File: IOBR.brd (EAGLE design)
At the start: 53.3 x 53.3 mm, 10 parts, among them J1 Digital_0_7, J10 Power, J2 Analog, J3 Digital_8_13

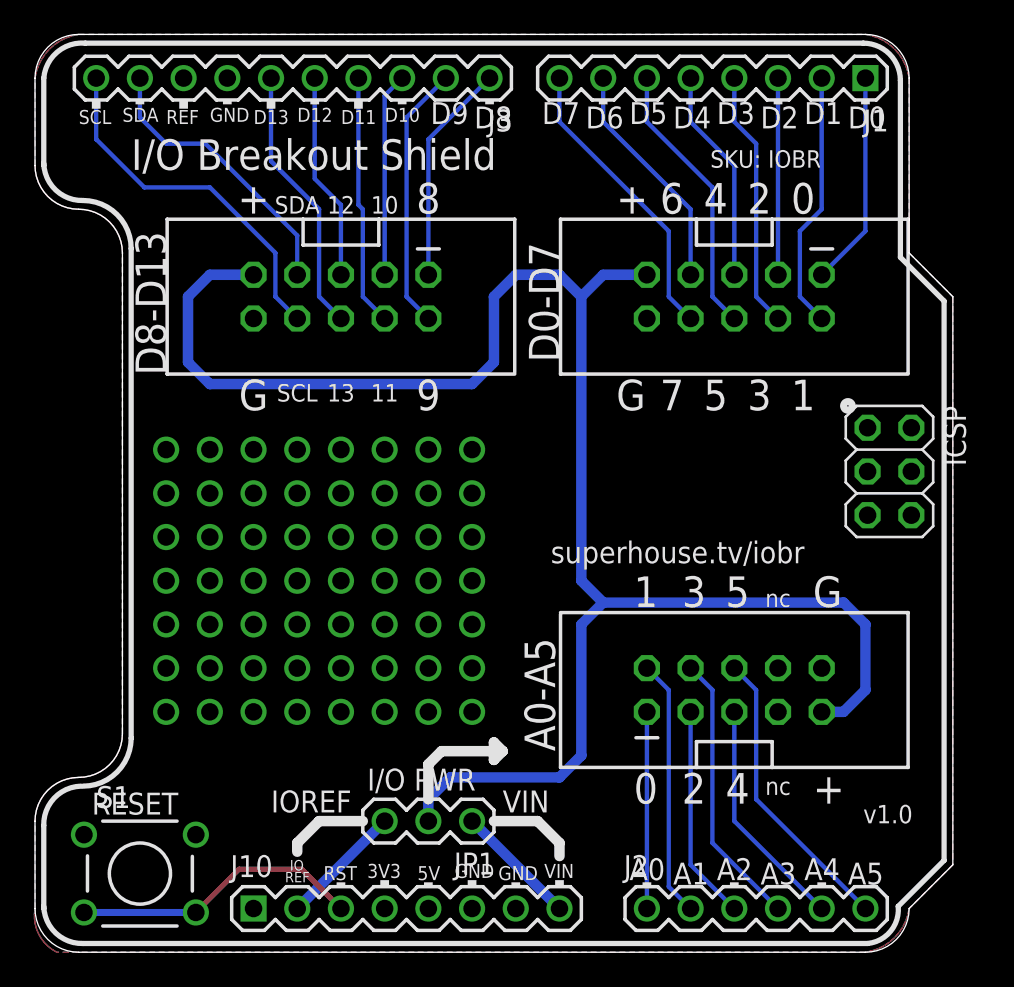
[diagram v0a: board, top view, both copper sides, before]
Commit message: Expanded headers to 2x6 to include IOREF and RESET for v2.0 release
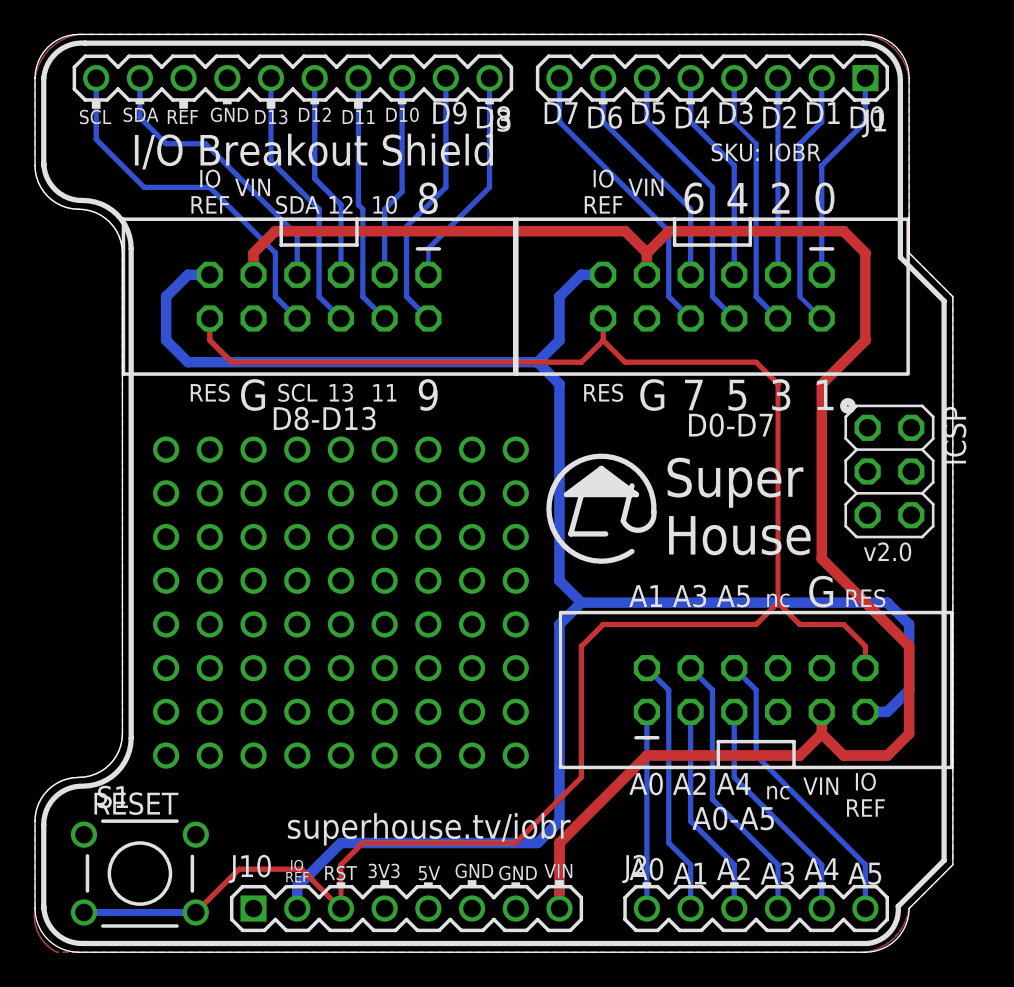
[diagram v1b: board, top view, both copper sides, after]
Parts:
- removed JP1: (no value), freetronics-master-v1.1:1X03
- JP11, JP13, JP15: value M05X2SHD -> M06X2; device freetronics-original:2X5-SHROUDED -> freetronics-jon:2X6-SHROUDED
- moved JP11 5.24 mm to (35.6, 14.0)
- moved JP13 5.24 mm to (45.7, 39.4)
- moved JP15 5.24 mm to (22.9, 39.4)
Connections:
- removed net IOVCC: JP1.2, JP11.9, JP13.9, JP15.9
- net IOREF: now also JP11.11, JP13.11, JP15.11; no longer JP1.3
- net RESET: now also JP11.12, JP13.12, JP15.12
- net VIN: now also JP11.9, JP13.9, JP15.9; no longer JP1.1
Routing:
- net IOVCC: track 102.8 -> 0.00 mm
- net IOREF: track 7.18 -> 107.9 mm
- net RESET: track 16.9 -> 113.4 mm
- net VIN: track 7.18 -> 100.4 mm
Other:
- board text added: "IO REF"
- board text added: "RES"
- board text added: "Super House"
- board text added: "v2.0"
- board text removed: "+"
- board text removed: "I/O PWR"
- board text removed: "VCC"
- board text removed: "v1.0"

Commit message: Converted parts to SuperHouse libraries
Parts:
- ICSP: device pinhead:2X03 -> SuperHouse-Connectors:2X03PTH
- J1: device freetronics:1X08 -> SuperHouse-Connectors:1X08
- J10: device freetronics-master-v1:1X08 -> SuperHouse-Connectors:1X08
- J2: device freetronics-master-v1:1X06 -> SuperHouse-Connectors:1X06
- J3: device freetronics-original:1X10 -> SuperHouse-Connectors:1X10
- JP11, JP13, JP15: value M06X2 -> M06X2-SHROUDED; device freetronics-jon:2X6-SHROUDED -> SuperHouse-Connectors:2X6-SHROUDED
- S1: device freetronics-master-v1:TACTILE-PTH -> SuperHouse-Switches:TACTILE-PTH-6MM

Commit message: Update for v2.1 release
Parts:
- removed ICSP: ICSP:MAIN, SuperHouse-Connectors:2X03PTH
- removed J10: Power, SuperHouse-Connectors:1X08
- removed JP11, JP13, JP15: M06X2-SHROUDED, SuperHouse-Connectors:2X6-SHROUDED
- added J4: Power, SuperHouse-Connectors:1X08-P-BELOW
- added J5: ICSP:MAIN, SuperHouse-Connectors:2X03-ICSP-ST-BELOW
- added J6, J7, J8: M02X6-SHROUDED, SuperHouse-Connectors:2X06-SHROUDED
- J1: device SuperHouse-Connectors:1X08 -> SuperHouse-Connectors:1X08-P-BELOW
- J2: device SuperHouse-Connectors:1X06 -> SuperHouse-Connectors:1X06-P-BELOW
- J3: device SuperHouse-Connectors:1X10 -> SuperHouse-Connectors:1X10-P-BELOW
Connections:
- net 3V3: now also J4.4; no longer J10.4
- net 5V: now also J4.5; no longer J10.5
- net A0: now also J8.1; no longer JP11.1
- net A1: now also J8.2; no longer JP11.2
- net A2: now also J8.3; no longer JP11.3
- net A3: now also J8.4; no longer JP11.4
- net A4: now also J8.5; no longer JP11.5
- net A5: now also J8.6; no longer JP11.6
- net D0_RX: now also J7.1; no longer JP13.1
- net D10: now also J6.3; no longer JP15.3
- net D11_MOSI: now also J6.4; no longer JP15.4
- net D12_MISO: now also J6.5; no longer JP15.5
- net D13_SCK: now also J6.6; no longer JP15.6
- net D1_TX: now also J7.2; no longer JP13.2
- net D2: now also J7.3; no longer JP13.3
- net D3: now also J7.4; no longer JP13.4
- net D4: now also J7.5; no longer JP13.5
- net D5: now also J7.6; no longer JP13.6
- net D6: now also J7.7; no longer JP13.7
- net D7: now also J7.8; no longer JP13.8
- net D8: now also J6.1; no longer JP15.1
- net D9: now also J6.2; no longer JP15.2
- net GND: now also J4.6, J4.7, J5.6, J6.10, J7.10, J8.10; no longer ICSP.6, J10.6, J10.7, JP11.10, JP13.10, JP15.10
- net IOREF: now also J4.2, J6.11, J7.11, J8.11; no longer J10.2, JP11.11, JP13.11, JP15.11
- net N$186: now also J5.1; no longer ICSP.1
- net N$187: now also J5.3; no longer ICSP.3
- net N$188: now also J5.5; no longer ICSP.5
- net N$197: now also J5.2; no longer ICSP.2
- net N$198: now also J5.4; no longer ICSP.4
- net RESET: now also J4.3, J6.12, J7.12, J8.12; no longer J10.3, JP11.12, JP13.12, JP15.12
- net SCL: now also J6.8; no longer JP15.8
- net SDA: now also J6.7; no longer JP15.7
- net VIN: now also J4.8, J6.9, J7.9, J8.9; no longer J10.8, JP11.9, JP13.9, JP15.9
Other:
- board text added: "(C)2019 SuperHouse Released under the TAPR Open Hardware License www.tapr.org/OHL"
- board text added: "v2.1"
- board text removed: "(C) 2017 SuperHouse Released under the TAPR Open Hardware License www.tapr.org/OHL"
- board text removed: "v2.0"
